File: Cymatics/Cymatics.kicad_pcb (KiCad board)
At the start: 2 copper layers, 65 x 70 mm, 79 parts, among them IC1 LMV358IDR, IC2 MAX7403CSA+, IC3 LMV358IDR, IC4 LMV358IDR, IC5 MAX7403CSA+, J1 Screw_Terminal_01x03, J10 Screw_Terminal_01x04, J11 Screw_Terminal_01x05, J12 Screw_Terminal_01x02, J13 Screw_Terminal_01x02, J14 RCU-0C, J15 Screw_Terminal_01x02, J16 Screw_Terminal_01x03, J17 Screw_Terminal_01x02, J18 Screw_Terminal_01x06, J19 RCU-0C, J2 Screw_Terminal_01x02, J20 RCU-0C, J21 RCU-0C, J22 RCU-0C, J23 RCU-0C, J24 RCU-0C, J3 Screw_Terminal_01x03, J4 Screw_Terminal_01x03, J5 Screw_Terminal_01x02, J6 Conn_01x16_Socket, J7 Conn_01x12_Socket, J8 Screw_Terminal_01x04, J9 Screw_Terminal_01x02, U1 SN74AHCT125DR, U2 MAX7480ESA+

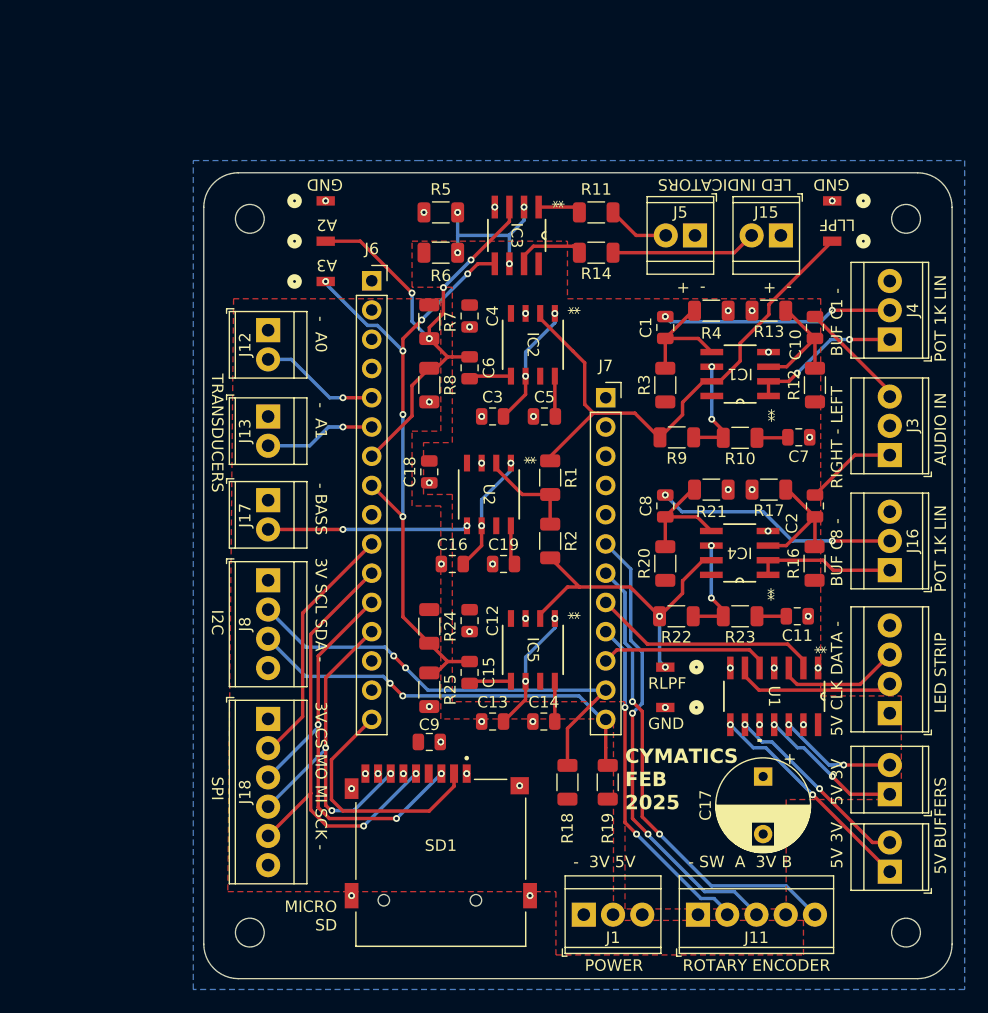
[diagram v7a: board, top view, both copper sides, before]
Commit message: changed positioning of blocks for diagrams
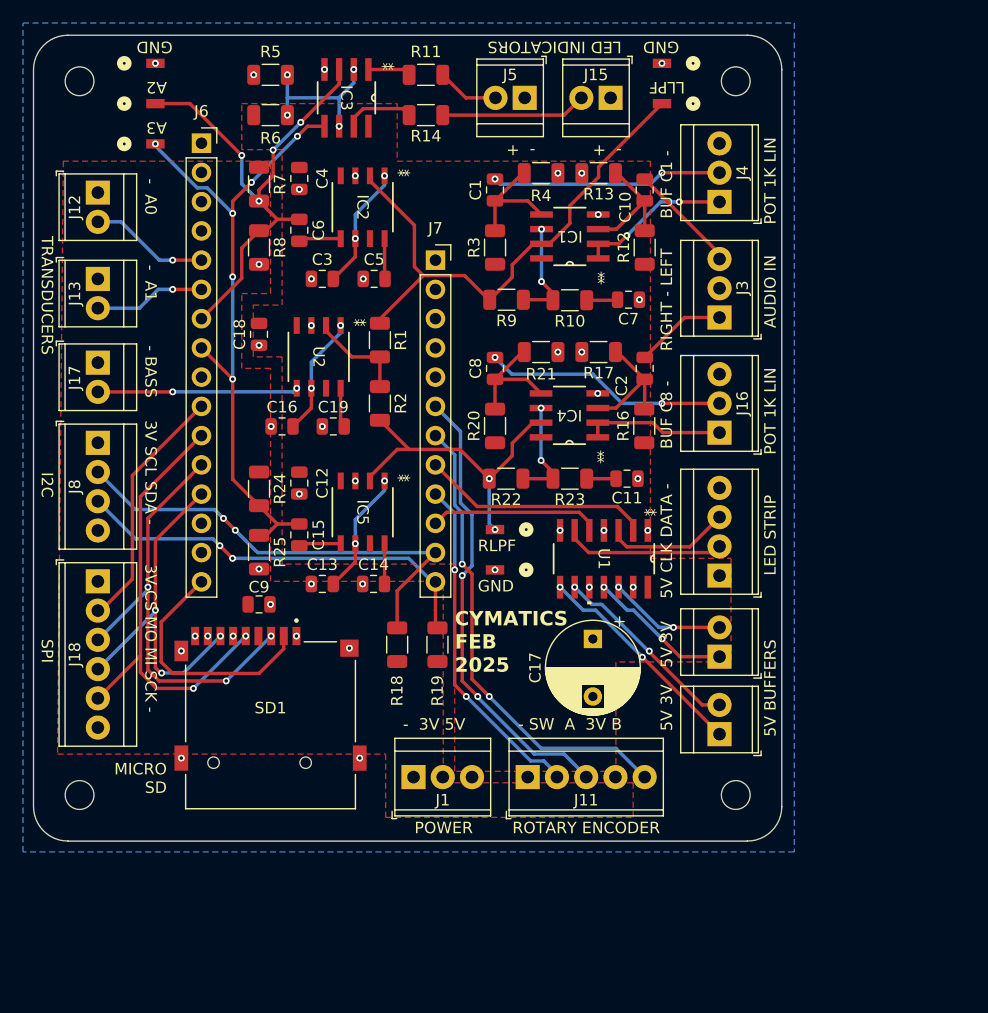
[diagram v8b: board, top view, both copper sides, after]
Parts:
- moved C7 19.0 mm to (141.8, 76.1)
- moved J5 19.0 mm to (132.8, 58.5)
- moved REF** 19.0 mm to (151.1, 119.1)
- moved REF** 19.0 mm to (151.1, 57.1)
- moved U1 19.0 mm to (139.7, 98.6)
- moved C12 19.0 mm to (113.2, 92.0)
- moved C15 19.0 mm to (113.2, 96.5)
- moved C16 19.0 mm to (111.7, 87.1)
- moved C18 19.0 mm to (109.7, 79.1)
- moved C4 19.0 mm to (113.2, 65.5)
- moved C6 19.0 mm to (113.2, 70.0)
- moved C9 19.0 mm to (109.7, 102.5)
- moved IC2 19.0 mm to (118.7, 68.0)
- moved IC5 19.0 mm to (118.7, 94.5)
- moved J12 19.0 mm to (95.7, 66.8)
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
